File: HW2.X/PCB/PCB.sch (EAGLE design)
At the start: 17 parts

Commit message: PCB Schematics
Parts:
- added J1, J2: (no value), ME433:CONN_08"
- added PICKIT3: (no value), ME433:CONN_05
- added U$6: USB_MB, ME433:USB_MB
- added U$7: SLIDESWITCH, ME433:SLIDESWITCH
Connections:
- removed net N$14: U$2.15.VBUS
- removed net N$19: U$2.21.D+
- removed net N$20: U$2.22.D-
- new net +5V: J2.2, U$7.1.5V
- new net B4: J1.4
- new net N$6: LED2.A, R4.1
- new net N$7: U$2.22.D-, U$6.2.D-
- new net N$8: U$2.21.D+, U$6.3.D+
- new net N$9: U$2.14.USBID, U$6.4.ID
- net +3V3: now also J1.2, PICKIT3.2
- net A0: now also J1.8
- net A1: now also J1.7
- net A4: now also J1.3; no longer LED2.A, U$2.12.A4
- net B13: now also J2.6
- net B14: now also J2.7
- net B15: now also J2.8
- net B2: now also J1.6
- net B3: now also J1.5
- net B7: now also J2.3
- net B8: now also J2.4
- net B9: now also J2.5
- net GND: now also J1.1, J2.1, LED2.C, PICKIT3.3, U$6.5.GND; no longer R4.2
- net N$2: now also R4.2, U$2.12.A4; no longer LED2.C, R4.1
- net N$3: now also PICKIT3.1
- net PGEC1: now also PICKIT3.5
- net PGED1: now also PICKIT3.4
- net VBUS: now also U$2.15.VBUS, U$6.1.VBUS, U$7.2.VBUS
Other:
- moved on the sheet: LED1, LED2, R3, R4

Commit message: Update schematics
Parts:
- removed PICKIT3: (no value), ME433:CONN_05
- added U$8: PICKIT3, ME433:PICKIT3
- renumbered U$4 to USER, U$5 to RESET
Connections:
- removed net PGEC1: PICKIT3.5, U$2.5.PGEC1
- removed net PGED1: PICKIT3.4, U$2.4.PGED1
- new net N$10: U$2.4.PGED1, U$8.4.PGEDX
- new net N$11: U$2.5.PGEC1, U$8.5.PGECX
- net +3V3: now also U$8.2.VDD; no longer PICKIT3.2
- net +5V: now also C2.1, U$1.2.VIN, U$2.15.VBUS
- net GND: now also R4.1, U$8.3.VSS; no longer LED2.C, PICKIT3.3
- net N$2: now also LED2.C; no longer U$2.12.A4
- net N$3: now also U$8.1.MCLR; no longer PICKIT3.1
- net N$6: now also U$2.12.A4; no longer R4.1
- net VBUS: no longer C2.1, U$1.2.VIN, U$2.15.VBUS
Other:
- moved on the sheet: J1, J2, LED2, R4

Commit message: PCB board arrangement of components
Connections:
- removed net N$12: R2.1, U$2.11.B4, USER.2
- removed net N$6: LED2.A, U$2.12.A4
- net A4: now also LED2.A, U$2.12.A4
- net B4: now also R2.1, U$2.11.B4, USER.2

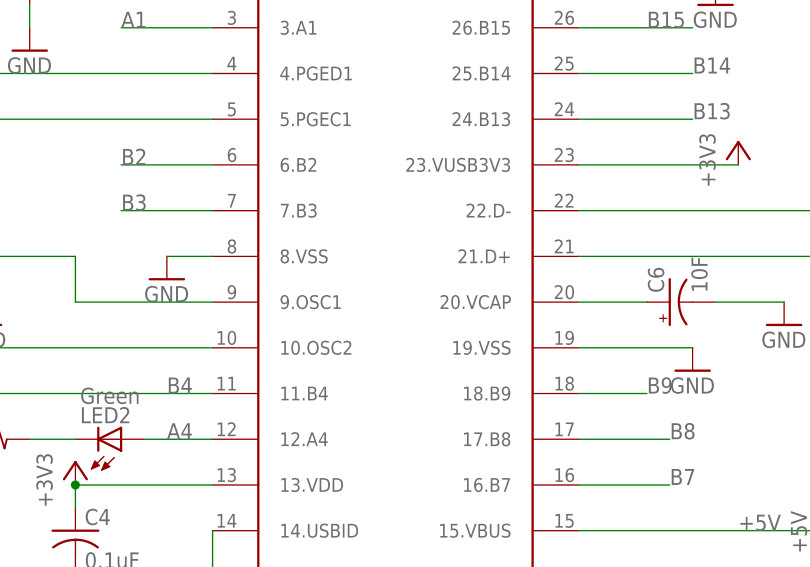
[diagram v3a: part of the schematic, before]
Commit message: PCB Fix component positions
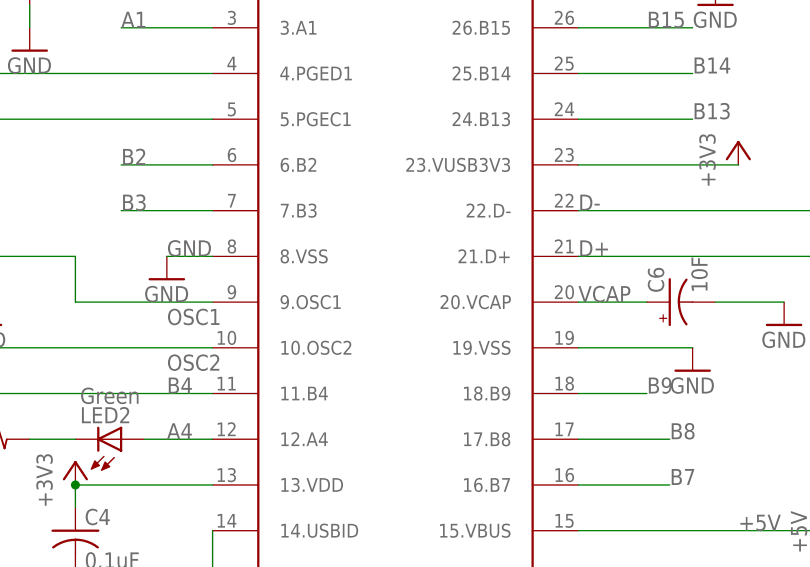
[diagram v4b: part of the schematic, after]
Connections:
- net N$10 renamed PEGD1
- net N$11 renamed PEGC1
- net N$18 renamed VCAP
- net N$3 renamed MCLR
- net N$4 renamed OSC1
- net N$5 renamed OSC2
- net N$7 renamed D-
- net N$8 renamed D+
- net N$9 renamed USBID
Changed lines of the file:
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@@
 <pinref part="GND5" gate="1" pin="GND"/>
 <wire x1="896.62" y1="711.2" x2="891.54" y2="711.2" width="0.1524" layer="91"/>
+<label x="891.54" y="711.2" size="1.778" layer="95"/>
 </segment>
 <segment>
@@
 </segment>
 </net>
-<net name="N$3" class="0">
+<net name="MCLR" class="0">
 <segment>
 <pinref part="R1" gate="G$1" pin="1"/>
@@
 </segment>
 </net>
-<net name="N$18" class="0">
+<net name="VCAP" class="0">
 <segment>
 <pinref part="U$2" gate="G$1" pin="20.VCAP"/>
 <pinref part="C6" gate="G$1" pin="+"/>
 <wire x1="937.26" y1="706.12" x2="944.88" y2="706.12" width="0.1524" layer="91"/>
+<label x="937.26" y="706.12" size="1.778" layer="95"/>
 </segment>
 </net>
@@
 </segment>
 </net>
-<net name="N$4" class="0">
+<net name="OSC1" class="0">
 <segment>
 <pinref part="U$3" gate="G$1" pin="1.OCS1"/>
@@
 <pinref part="U$2" gate="G$1" pin="9.OSC1"/>
 <wire x1="881.38" y1="706.12" x2="896.62" y2="706.12" width="0.1524" layer="91"/>
-</segment>
-</net>
-<net name="N$5" class="0">
+<label x="891.54" y="703.58" size="1.778" layer="95"/>
+</segment>
+</net>
+<net name="OSC2" class="0">
 <segment>
 <pinref part="U$3" gate="G$1" pin="3.OCS2"/>
 <pinref part="U$2" gate="G$1" pin="10.OSC2"/>
 <wire x1="866.14" y1="701.04" x2="896.62" y2="701.04" width="0.1524" layer="91"/>
-</segment>
-</net>
-<net name="N$7" class="0">
+<label x="891.54" y="698.5" size="1.778" layer="95"/>
+</segment>
+</net>
+<net name="D-" class="0">
 <segment>
 <pinref part="U$6" gate="G$1" pin="2.D-"/>
 <pinref part="U$2" gate="G$1" pin="22.D-"/>
 <wire x1="993.14" y1="716.28" x2="937.26" y2="716.28" width="0.1524" layer="91"/>
-</segment>
-</net>
-<net name="N$8" class="0">
+<label x="937.26" y="716.28" size="1.778" layer="95"/>
+</segment>
+</net>
+<net name="D+" class="0">
 <segment>
 <pinref part="U$6" gate="G$1" pin="3.D+"/>
 <pinref part="U$2" gate="G$1" pin="21.D+"/>
 <wire x1="993.14" y1="711.2" x2="937.26" y2="711.2" width="0.1524" layer="91"/>
-</segment>
-</net>
-<net name="N$9" class="0">
+<label x="937.26" y="711.2" size="1.778" layer="95"/>
+</segment>
+</net>
+<net name="USBID" class="0">
 <segment>
 <pinref part="U$6" gate="G$1" pin="4.ID"/>
@@
 </segment>
 </net>
-<net name="N$10" class="0">
+<net name="PEGD1" class="0">
 <segment>
 <pinref part="U$8" gate="G$1" pin="4.PGEDX"/>
@@
 </segment>
 </net>
-<net name="N$11" class="0">
+<net name="PEGC1" class="0">
 <segment>
 <pinref part="U$8" gate="G$1" pin="5.PGECX"/>
